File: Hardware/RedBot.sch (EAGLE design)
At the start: 53 parts, among them IC1 FT232RLSSOP, J1 5.5x2.1mm Barrel, J2 AVR_SPI_PRG_6PTH, U1 ATMEGA328P, U2 TB6612FNG, U3 MIC5219 5V, U4 MIC5219 3.3V, X1 USB-B, Y1 16MHz

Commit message: v01 files as sent to protos
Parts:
- removed J1: 5.5x2.1mm Barrel, SparkFun-Connectors:POWER_JACKSMD
- removed J2: AVR_SPI_PRG_6PTH, SparkFun-Connectors:AVR_SPI_PRG_6PTH
- removed X1: USB-B, SparkFun-Connectors:USBPTH
- added JP13: (no value), SparkFun-Connectors:M03X2SMT
- added SFE-LOGO1: LOGO-SFENEW, SparkFun-Aesthetics:LOGO-SFENEW
- added STANDOFF1, STANDOFF2, STANDOFF3, STANDOFF4: STAND-OFF, SparkFun-Electromechanical:STAND-OFF
- added U$17: OSHW-LOGOS, SparkFun-Aesthetics:OSHW-LOGOS
- JP3: value STAND-OFF -> 5.5x2.1mm Barrel; device SparkFun-Electromechanical:STAND-OFF -> SparkFun-Connectors:POWER_JACKSMD
- JP4: value STAND-OFF -> USB-B; device SparkFun-Electromechanical:STAND-OFF -> SparkFun-Connectors:USB-MINIB-5PIN
- JP5: value STAND-OFF -> AVR_SPI_PRG_6PTH; device SparkFun-Electromechanical:STAND-OFF -> SparkFun-Connectors:AVR_SPI_PRG_6PTH
- JP6: value STAND-OFF -> M05X2PTH; device SparkFun-Electromechanical:STAND-OFF -> SparkFun-Connectors:M05X2PTH
- JP7: value (none) -> M05X2PTH; device SparkFun-Connectors:M03X2SMT -> SparkFun-Connectors:M05X2PTH
- renumbered IC1 to U5
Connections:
- new net N$6: JP4.MTN1, JP4.MTN2, JP4.MTN3, JP4.MTN4
- net 5V: now also JP13.3, JP13.4, JP5.2, JP6.1, JP6.3, JP6.5, JP6.7, JP6.9, JP7.1, JP7.3, JP7.5, JP7.7, JP7.9; no longer J2.2, JP9.3, JP9.4
- net GND: now also JP13.5, JP13.6, JP3.GND, JP4.GND, JP5.6, JP6.10, JP6.2, JP6.4, JP6.6, JP6.8, JP7.10, JP7.2, JP7.4, JP7.8; no longer J1.GND, J2.6, JP7.5, X1.GND
- net MISO: now also JP5.1; no longer J2.1
- net N$26: now also JP4.D-; no longer X1.D-
- net N$27: now also JP4.D+; no longer X1.D+
- net RESET: now also JP5.5; no longer J2.5
- net SCK: now also JP5.3; no longer J2.3
- net SENSOR_0/SW_TXO: now also JP10.1; no longer JP9.1
- net SENSOR_1/SW_RXI: now also JP10.2; no longer JP9.2
- net SENSOR_2: now also JP11.1; no longer JP10.1
- net SENSOR_3: now also JP11.2; no longer JP10.2
- net SENSOR_4: now also JP12.1; no longer JP11.1
- net SENSOR_5: now also JP12.2; no longer JP11.2
- net SENSOR_6: now also JP13.1; no longer JP12.1
- net SENSOR_7: now also JP13.2; no longer JP12.2
- net SERVO_1: now also JP8.1; no longer JP7.1
- net SERVO_2: now also JP8.2; no longer JP7.2
- net SERVO_3: now also JP9.1; no longer JP8.1
- net SERVO_4/MOSI: now also JP5.4, JP9.2; no longer J2.4, JP8.2
- net V_BATT: now also JP3.PWR, JP9.3, JP9.4; no longer J1.PWR, JP7.3, JP7.4
- net V_USB: now also JP4.VBUS; no longer X1.VBUS
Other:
- note added: "01"
- note added: "M.Hord"
- moved on the sheet: JP10, JP11, JP12, JP8, JP9

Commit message: v02 hardware file commit
Initial protos are messed up- no internal copper layers.
Took this opportunity to add a couple of new features:
- .1" headers for input voltage and motor connections
- PMOS switch to disconnect servos when powered down
- fixed barrel jack so the right pin is to ground
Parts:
- added JP14, JP15: (no value), SparkFun-Connectors:M02PTH
- added Q1: (no value), SparkFun-DiscreteSemi:IRF7509
- added R11: 10k, SparkFun-Resistors:10KOHM1/10W1%(0603)
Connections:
- new net N$2: Q1NMOS.D, Q1PMOS.G, R11.1
- new net V_GATED: JP8.3, JP8.4, JP9.3, JP9.4, Q1PMOS.S
- net GND: now also JP3.GNDBREAK, Q1NMOS.S
- net L01: now also JP1.3, JP15.2
- net L02: now also JP15.1
- net PROGRAM_ENABLE: now also Q1NMOS.G
- net R01: now also JP14.2, JP2.1
- net R02: now also JP14.1
- net V_BATT: now also Q1PMOS.D, R11.2; no longer JP8.3, JP8.4, JP9.3, JP9.4
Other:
- note added: "02"
- note removed: "01"
- moved on the sheet: D1, D2, JP3, R4, S3, U3, U4

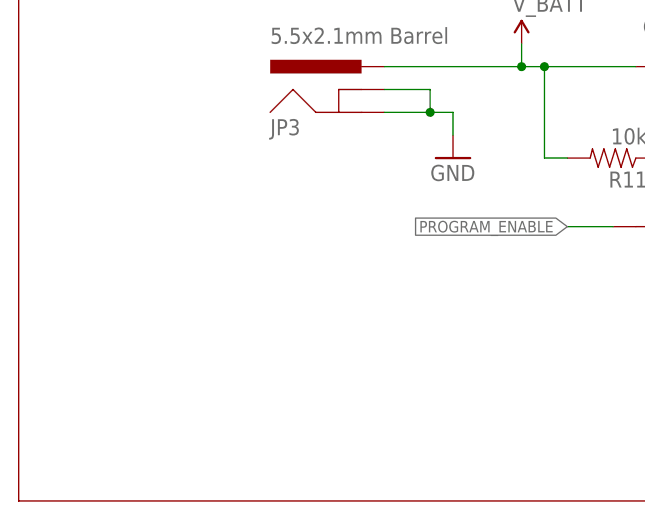
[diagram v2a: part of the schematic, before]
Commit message: Last commit incomplete; this adds header for PS
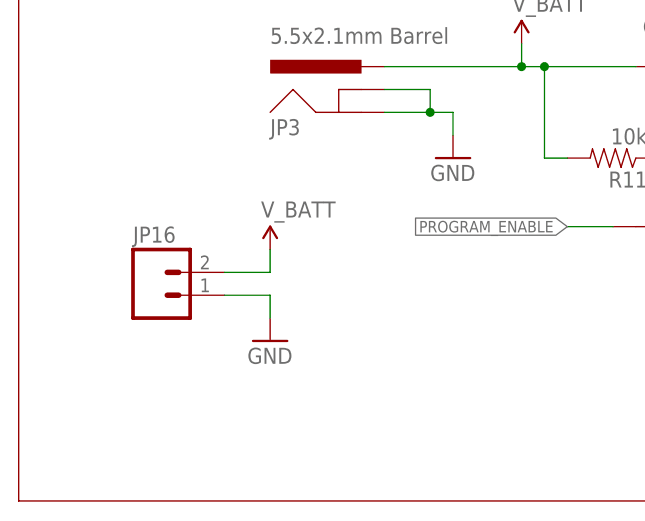
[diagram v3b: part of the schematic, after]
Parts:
- added JP16: (no value), SparkFun-Connectors:M02PTH
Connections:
- net GND: now also JP16.1
- net V_BATT: now also JP16.2
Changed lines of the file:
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@@
 <part name="V_GATE1" library="SparkFun-Aesthetics" deviceset="V_BATT" device="" value="V_GATED"/>
 <part name="U$4" library="SparkFun-Aesthetics" deviceset="V_BATT" device=""/>
+<part name="JP16" library="SparkFun-Connectors" deviceset="M02" device="PTH"/>
+<part name="GND21" library="SparkFun-Aesthetics" deviceset="GND" device=""/>
+<part name="U$6" library="SparkFun-Aesthetics" deviceset="V_BATT" device=""/>
 </parts>
 <sheets>
@@
 <instance part="V_GATE1" gate="G$1" x="83.82" y="50.8"/>
 <instance part="U$4" gate="G$1" x="106.68" y="50.8"/>
+<instance part="JP16" gate="G$1" x="15.24" y="22.86"/>
+<instance part="GND21" gate="1" x="27.94" y="17.78"/>
+<instance part="U$6" gate="G$1" x="27.94" y="27.94"/>
 </instances>
 <busses>
@@
 <wire x1="132.08" y1="43.18" x2="134.62" y2="43.18" width="0.1524" layer="91"/>
 </segment>
+<segment>
+<pinref part="JP16" gate="G$1" pin="1"/>
+<pinref part="GND21" gate="1" pin="GND"/>
+<wire x1="22.86" y1="22.86" x2="27.94" y2="22.86" width="0.1524" layer="91"/>
+<wire x1="27.94" y1="22.86" x2="27.94" y2="20.32" width="0.1524" layer="91"/>
+</segment>
 </net>
 <net name="5V" class="0">
@@
 <pinref part="U$4" gate="G$1" pin="V_BATT"/>
 </segment>
-</net>
+<segment>
+<pinref part="JP16" gate="G$1" pin="2"/>
+<wire x1="22.86" y1="25.4" x2="27.94" y2="25.4" width="0.1524" layer="91"/>
+<wire x1="27.94" y1="25.4" x2="27.94" y2="27.94" width="0.1524" layer="91"/>
+<pinref part="U$6" gate="G$1" pin="V_BATT"/>
+</segment>
+</net>

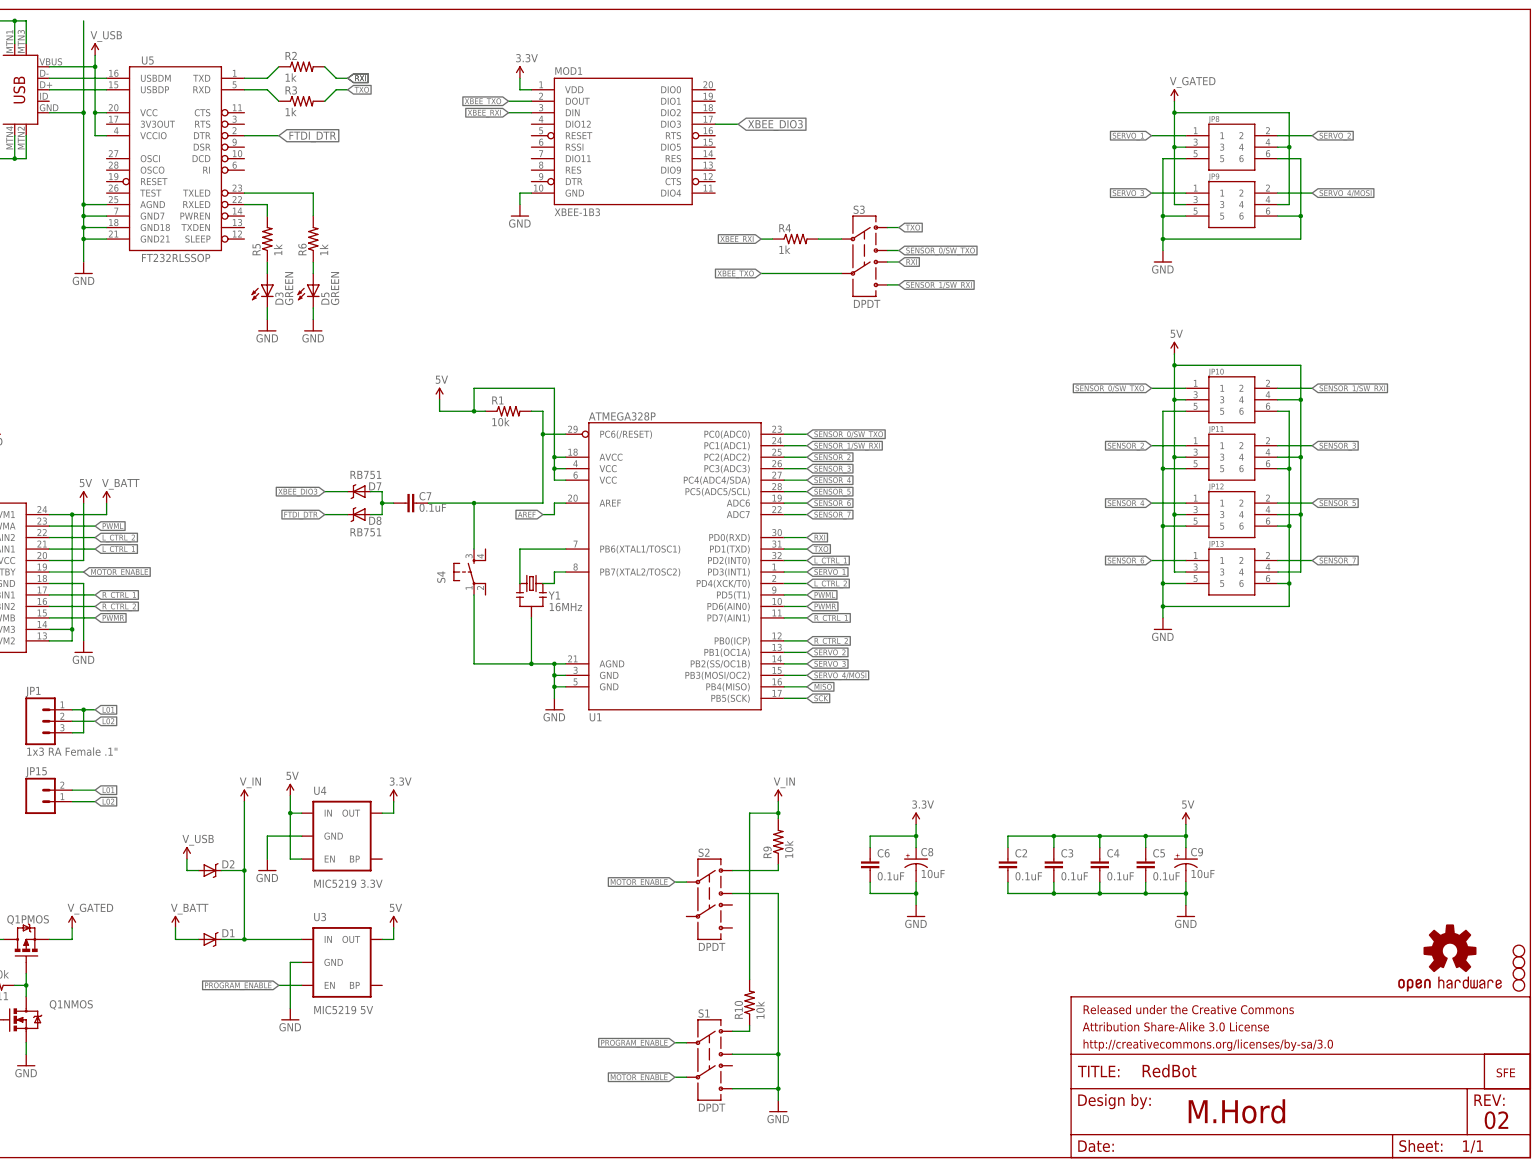
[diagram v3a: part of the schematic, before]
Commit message: Fix a couple of problems: - TEST pin on FTDI chip needs to be grounded. - FTDI chip not properly bypassed.
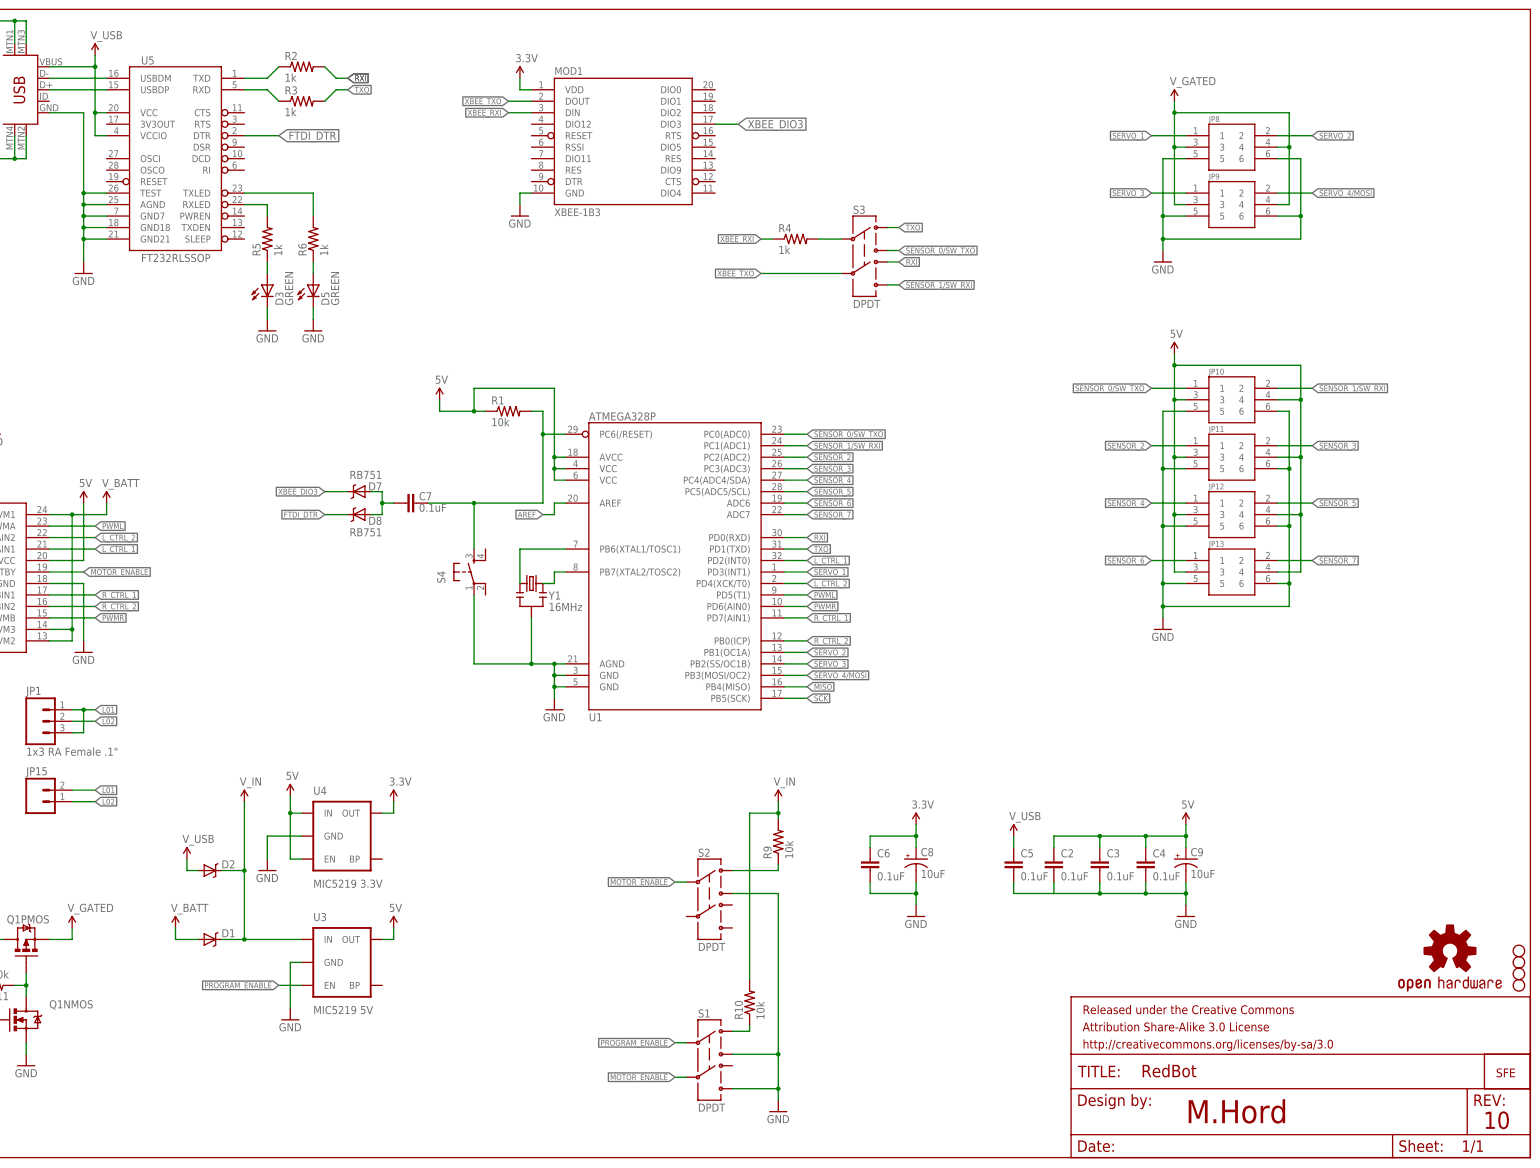
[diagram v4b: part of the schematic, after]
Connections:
- net 5V: no longer C5.1
- net GND: now also U5.TEST
- net V_USB: now also C5.1
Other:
- note added: "10"
- note removed: "02"
- moved on the sheet: C2, C3, C4, C5
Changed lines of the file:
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@@
 <part name="GND21" library="SparkFun-Aesthetics" deviceset="GND" device=""/>
 <part name="U$6" library="SparkFun-Aesthetics" deviceset="V_BATT" device=""/>
+<part name="U$19" library="SparkFun-Aesthetics" deviceset="5V" device="" value="V_USB"/>
 </parts>
 <sheets>
@@
 <wire x1="0" y1="254" x2="0" y2="0" width="0.1524" layer="94"/>
 <text x="330.2" y="7.62" size="5.08" layer="94">M.Hord</text>
-<text x="395.986" y="6.35" size="3.81" layer="94">02</text>
+<text x="395.986" y="6.35" size="3.81" layer="94">10</text>
 </plain>
 <instances>
 <instance part="FRAME1" gate="G$2" x="304.8" y="0"/>
 <instance part="U1" gate="G$1" x="215.9" y="134.62"/>
-<instance part="C2" gate="G$1" x="290.83" y="63.5"/>
-<instance part="C3" gate="G$1" x="300.99" y="63.5"/>
+<instance part="C2" gate="G$1" x="300.99" y="63.5"/>
+<instance part="C3" gate="G$1" x="311.15" y="63.5"/>
 <instance part="R1" gate="G$1" x="180.34" y="165.1"/>
 <instance part="U5" gate="G$1" x="106.68" y="220.98"/>
 <instance part="U2" gate="G$1" x="63.5" y="129.54"/>
 <instance part="JP3" gate="G$1" x="38.1" y="40.64"/>
-<instance part="C4" gate="G$1" x="311.15" y="63.5"/>
-<instance part="C5" gate="G$1" x="321.31" y="63.5"/>
+<instance part="C4" gate="G$1" x="321.31" y="63.5"/>
+<instance part="C5" gate="G$1" x="292.1" y="63.5"/>
 <instance part="C6" gate="G$1" x="260.35" y="63.5"/>
 <instance part="S1" gate="G$1" x="224.79" y="22.86"/>
@@
 <instance part="GND21" gate="1" x="27.94" y="17.78"/>
 <instance part="U$6" gate="G$1" x="27.94" y="27.94"/>
+<instance part="U$19" gate="G$1" x="292.1" y="71.12"/>
 </instances>
 <busses>
@@
 <wire x1="78.74" y1="231.14" x2="86.36" y2="231.14" width="0.1524" layer="91"/>
 <pinref part="U5" gate="G$1" pin="AGND"/>
-<wire x1="86.36" y1="231.14" x2="86.36" y2="210.82" width="0.1524" layer="91"/>
+<wire x1="86.36" y1="231.14" x2="86.36" y2="213.36" width="0.1524" layer="91"/>
+<wire x1="86.36" y1="213.36" x2="86.36" y2="210.82" width="0.1524" layer="91"/>
 <wire x1="86.36" y1="210.82" x2="91.44" y2="210.82" width="0.1524" layer="91"/>
 <pinref part="U5" gate="G$1" pin="GND7"/>
@@
 <wire x1="91.44" y1="203.2" x2="86.36" y2="203.2" width="0.1524" layer="91"/>
 <junction x="86.36" y="203.2"/>
-<wire x1="86.36" y1="251.46" x2="86.36" y2="231.14" width="0.1524" layer="91"/>
-<junction x="86.36" y="231.14"/>
+<pinref part="U5" gate="G$1" pin="TEST"/>
+<wire x1="91.44" y1="213.36" x2="86.36" y2="213.36" width="0.1524" layer="91"/>
+<junction x="86.36" y="213.36"/>
 </segment>
 <segment>
@@
 <wire x1="330.2" y1="58.42" x2="321.31" y2="58.42" width="0.1524" layer="91"/>
 <wire x1="321.31" y1="58.42" x2="311.15" y2="58.42" width="0.1524" layer="91"/>
-<wire x1="311.15" y1="58.42" x2="300.99" y2="58.42" width="0.1524" layer="91"/>
-<wire x1="300.99" y1="58.42" x2="290.83" y2="58.42" width="0.1524" layer="91"/>
+<wire x1="311.15" y1="58.42" x2="302.26" y2="58.42" width="0.1524" layer="91"/>
 <pinref part="C2" gate="G$1" pin="2"/>
-<wire x1="290.83" y1="60.96" x2="290.83" y2="58.42" width="0.1524" layer="91"/>
+<wire x1="302.26" y1="58.42" x2="300.99" y2="58.42" width="0.1524" layer="91"/>
+<wire x1="300.99" y1="60.96" x2="300.99" y2="58.42" width="0.1524" layer="91"/>
 <pinref part="C3" gate="G$1" pin="2"/>
-<wire x1="300.99" y1="60.96" x2="300.99" y2="58.42" width="0.1524" layer="91"/>
-<junction x="300.99" y="58.42"/>
-<pinref part="C4" gate="G$1" pin="2"/>
 <wire x1="311.15" y1="60.96" x2="311.15" y2="58.42" width="0.1524" layer="91"/>
 <junction x="311.15" y="58.42"/>
-<pinref part="C5" gate="G$1" pin="2"/>
+<pinref part="C4" gate="G$1" pin="2"/>
 <wire x1="321.31" y1="60.96" x2="321.31" y2="58.42" width="0.1524" layer="91"/>
 <junction x="321.31" y="58.42"/>
+<pinref part="C5" gate="G$1" pin="2"/>
+<wire x1="292.1" y1="60.96" x2="292.1" y2="58.42" width="0.1524" layer="91"/>
+<wire x1="292.1" y1="58.42" x2="300.99" y2="58.42" width="0.1524" layer="91"/>
 </segment>
 <segment>
@@
 <wire x1="321.31" y1="71.12" x2="311.15" y2="71.12" width="0.1524" layer="91"/>
 <wire x1="311.15" y1="71.12" x2="300.99" y2="71.12" width="0.1524" layer="91"/>
-<wire x1="300.99" y1="71.12" x2="290.83" y2="71.12" width="0.1524" layer="91"/>
 <junction x="330.2" y="71.12"/>
 <pinref part="C2" gate="G$1" pin="1"/>
-<wire x1="290.83" y1="68.58" x2="290.83" y2="71.12" width="0.1524" layer="91"/>
+<wire x1="300.99" y1="68.58" x2="300.99" y2="71.12" width="0.1524" layer="91"/>
 <pinref part="C3" gate="G$1" pin="1"/>
-<wire x1="300.99" y1="68.58" x2="300.99" y2="71.12" width="0.1524" layer="91"/>
-<junction x="300.99" y="71.12"/>
-<pinref part="C4" gate="G$1" pin="1"/>
 <wire x1="311.15" y1="68.58" x2="311.15" y2="71.12" width="0.1524" layer="91"/>
 <junction x="311.15" y="71.12"/>
-<pinref part="C5" gate="G$1" pin="1"/>
+<pinref part="C4" gate="G$1" pin="1"/>
 <wire x1="321.31" y1="68.58" x2="321.31" y2="71.12" width="0.1524" layer="91"/>
 <junction x="321.31" y="71.12"/>
@@
 <wire x1="109.22" y1="63.5" x2="111.76" y2="63.5" width="0.1524" layer="91"/>
 </segment>
-</net>
+<segment>
+<pinref part="C5" gate="G$1" pin="1"/>
+<pinref part="U$19" gate="G$1" pin="5V"/>
+<wire x1="292.1" y1="71.12" x2="292.1" y2="68.58" width="0.1524" layer="91"/>
+</segment>
+</net>
